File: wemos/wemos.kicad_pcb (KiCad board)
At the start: 2 copper layers, 9 parts, among them SW1 SW_SPST, U1 wemos

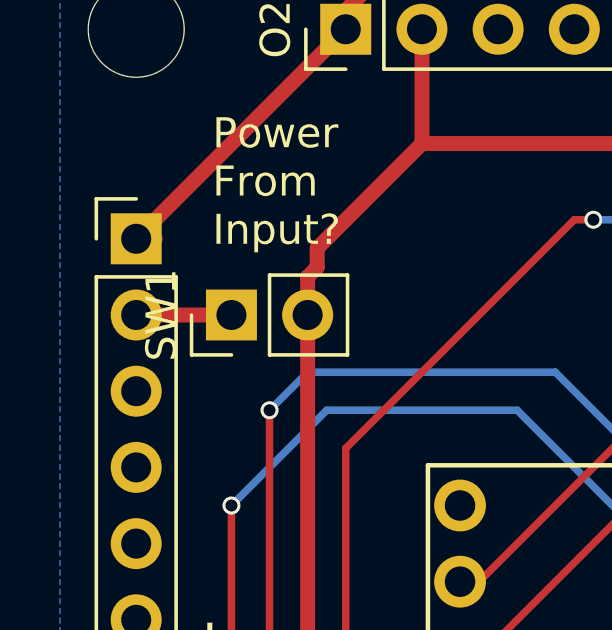
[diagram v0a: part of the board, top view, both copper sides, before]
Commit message: More update to make the libraryies use only relative paths.
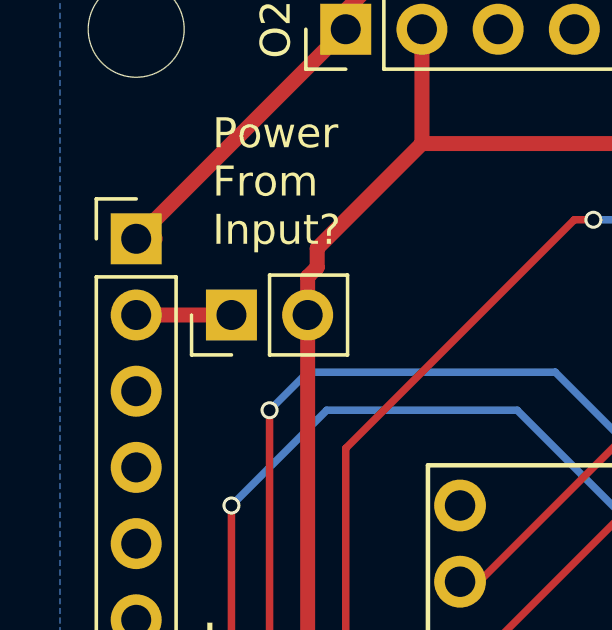
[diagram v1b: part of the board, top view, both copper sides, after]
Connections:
- net Earth renamed /GND
